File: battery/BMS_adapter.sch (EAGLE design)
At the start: 20 parts, among them J1 1376357-3

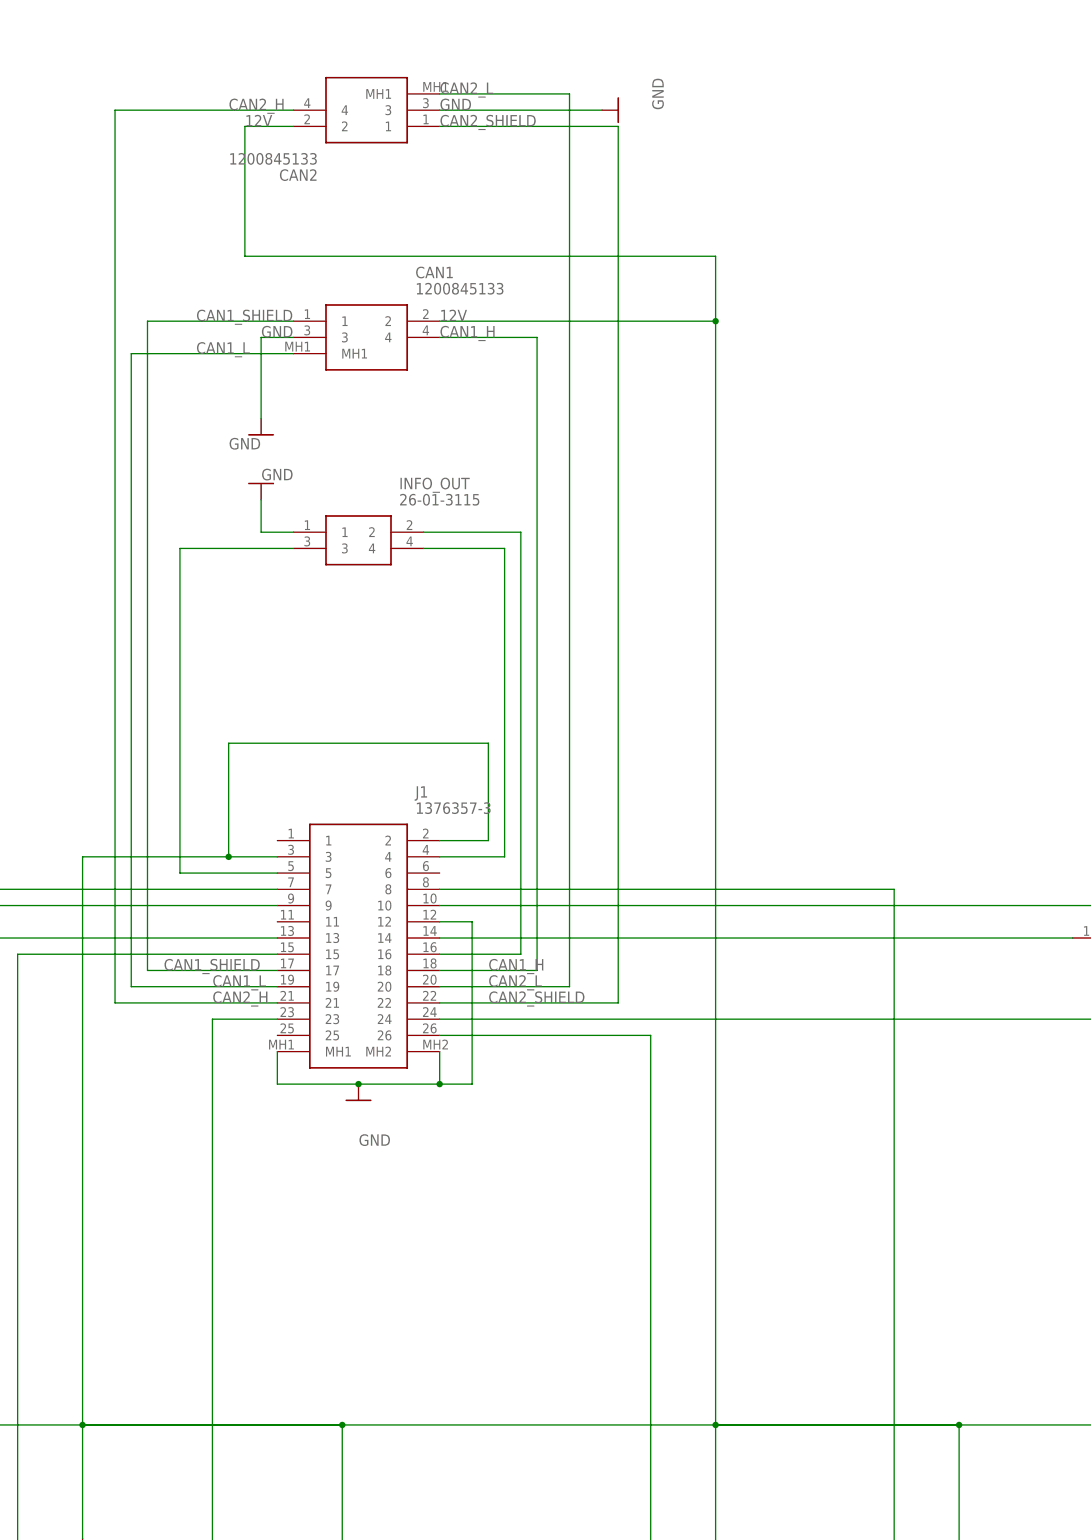
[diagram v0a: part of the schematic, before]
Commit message: changed linus' files to use the new BMS footprints.
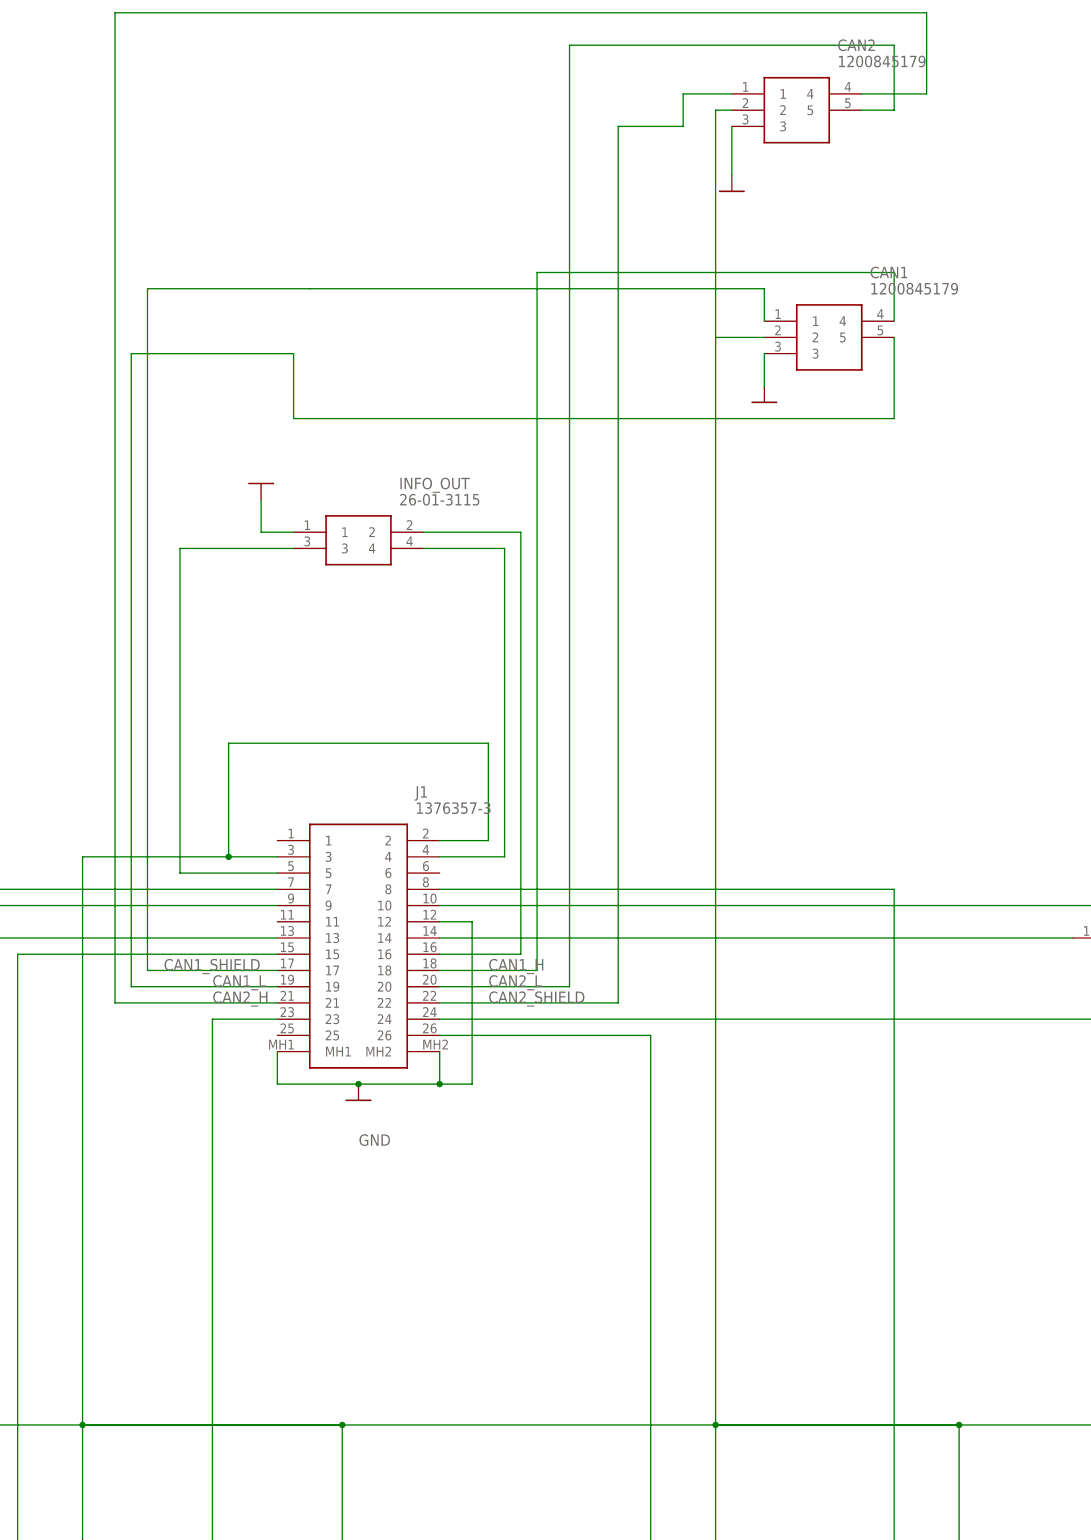
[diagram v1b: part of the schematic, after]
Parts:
- CAN1, CAN2: value 1200845133 -> 1200845179; device SamacSys_Parts:1200845133 -> SamacSys_Parts:1200845179
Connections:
- net CAN1_L: now also CAN1.5; no longer CAN1.MH1
- net CAN2_L: now also CAN2.5; no longer CAN2.MH1
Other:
- moved on the sheet: CAN1, CAN2
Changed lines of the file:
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@@
 <?xml version="1.0" encoding="utf-8"?>
 <!DOCTYPE eagle SYSTEM "eagle.dtd">
-<eagle version="9.1.1">
+<eagle version="9.1.3">
 <drawing>
 <settings>
@@
 <part name="MPO3" library="SamacSys_Parts" deviceset="26-01-3114" device=""/>
 <part name="MPO4" library="SamacSys_Parts" deviceset="26-01-3114" device=""/>
-<part name="CAN1" library="SamacSys_Parts" deviceset="1200845133" device=""/>
-<part name="GND2" library="SparkFun-PowerSymbols" library_urn="urn:adsk.eagle:library:530" deviceset="GND" device=""/>
-<part name="CAN2" library="SamacSys_Parts" deviceset="1200845133" device=""/>
-<part name="GND5" library="SparkFun-PowerSymbols" library_urn="urn:adsk.eagle:library:530" deviceset="GND" device=""/>
+<part name="CAN2" library="SamacSys_Parts" deviceset="1200845179" device=""/>
+<part name="CAN1" library="SamacSys_Parts" deviceset="1200845179" device=""/>
+<part name="GND6" library="SparkFun-PowerSymbols" library_urn="urn:adsk.eagle:library:530" deviceset="GND" device=""/>
+<part name="GND7" library="SparkFun-PowerSymbols" library_urn="urn:adsk.eagle:library:530" deviceset="GND" device=""/>
 </parts>
 <sheets>
@@
 <attribute name="VALUE" x="110.49" y="147.32" size="1.778" layer="96" align="center-left"/>
 </instance>
-<instance part="GND3" gate="1" x="88.9" y="149.86" smashed="yes" rot="R180">
-<attribute name="VALUE" x="86.36" y="155.194" size="1.778" layer="96" rot="R180" align="top-center"/>
-</instance>
+<instance part="GND3" gate="1" x="88.9" y="149.86" smashed="yes" rot="R180"/>
 <instance part="MPO3" gate="G$1" x="236.22" y="83.82" smashed="yes">
 <attribute name="NAME" x="252.73" y="91.44" size="1.778" layer="95" align="center-left"/>
@@
 <attribute name="VALUE" x="252.73" y="71.12" size="1.778" layer="96" align="center-left"/>
 </instance>
-<instance part="CAN1" gate="G$1" x="93.98" y="175.26" smashed="yes">
-<attribute name="NAME" x="113.03" y="182.88" size="1.778" layer="95" align="center-left"/>
-<attribute name="VALUE" x="113.03" y="180.34" size="1.778" layer="96" align="center-left"/>
-</instance>
-<instance part="GND2" gate="1" x="88.9" y="157.48" smashed="yes">
-<attribute name="VALUE" x="91.44" y="152.146" size="1.778" layer="96" align="top-center"/>
-</instance>
-<instance part="CAN2" gate="G$1" x="116.84" y="205.74" smashed="yes" rot="R180">
-<attribute name="NAME" x="97.79" y="198.12" size="1.778" layer="95" rot="R180" align="center-left"/>
-<attribute name="VALUE" x="97.79" y="200.66" size="1.778" layer="96" rot="R180" align="center-left"/>
-</instance>
-<instance part="GND5" gate="1" x="144.78" y="208.28" smashed="yes" rot="R90">
-<attribute name="VALUE" x="150.114" y="210.82" size="1.778" layer="96" rot="R90" align="top-center"/>
-</instance>
+<instance part="CAN2" gate="G$1" x="162.56" y="210.82"/>
+<instance part="CAN1" gate="G$1" x="167.64" y="175.26"/>
+<instance part="GND6" gate="1" x="162.56" y="195.58" smashed="yes"/>
+<instance part="GND7" gate="1" x="167.64" y="162.56" smashed="yes"/>
 </instances>
 <busses>
@@
 </segment>
 <segment>
-<pinref part="GND2" gate="1" pin="GND"/>
+<pinref part="CAN2" gate="G$1" pin="3"/>
+<wire x1="162.56" y1="205.74" x2="162.56" y2="198.12" width="0.1524" layer="91"/>
+<pinref part="GND6" gate="1" pin="GND"/>
+</segment>
+<segment>
 <pinref part="CAN1" gate="G$1" pin="3"/>
-<wire x1="93.98" y1="172.72" x2="88.9" y2="172.72" width="0.1524" layer="91"/>
-<wire x1="88.9" y1="172.72" x2="88.9" y2="160.02" width="0.1524" layer="91"/>
-<label x="88.9" y="172.72" size="1.778" layer="95"/>
-</segment>
-<segment>
-<pinref part="GND5" gate="1" pin="GND"/>
-<pinref part="CAN2" gate="G$1" pin="3"/>
-<wire x1="116.84" y1="208.28" x2="142.24" y2="208.28" width="0.1524" layer="91"/>
-<label x="116.84" y="208.28" size="1.778" layer="95"/>
+<wire x1="167.64" y1="170.18" x2="167.64" y2="165.1" width="0.1524" layer="91"/>
+<pinref part="GND7" gate="1" pin="GND"/>
 </segment>
 </net>
@@
 <wire x1="17.78" y1="-17.78" x2="17.78" y2="2.54" width="0.1524" layer="91"/>
 <wire x1="60.96" y1="91.44" x2="60.96" y2="2.54" width="0.1524" layer="91"/>
+<wire x1="160.02" y1="2.54" x2="160.02" y2="172.72" width="0.1524" layer="91"/>
+<wire x1="160.02" y1="172.72" x2="160.02" y2="208.28" width="0.1524" layer="91"/>
+<pinref part="CAN2" gate="G$1" pin="2"/>
+<wire x1="160.02" y1="208.28" x2="162.56" y2="208.28" width="0.1524" layer="91"/>
 <pinref part="CAN1" gate="G$1" pin="2"/>
-<wire x1="160.02" y1="2.54" x2="160.02" y2="175.26" width="0.1524" layer="91"/>
-<wire x1="160.02" y1="175.26" x2="116.84" y2="175.26" width="0.1524" layer="91"/>
-<pinref part="CAN2" gate="G$1" pin="2"/>
-<wire x1="93.98" y1="205.74" x2="86.36" y2="205.74" width="0.1524" layer="91"/>
-<wire x1="86.36" y1="205.74" x2="86.36" y2="185.42" width="0.1524" layer="91"/>
-<wire x1="86.36" y1="185.42" x2="160.02" y2="185.42" width="0.1524" layer="91"/>
-<wire x1="160.02" y1="185.42" x2="160.02" y2="175.26" width="0.1524" layer="91"/>
-<junction x="160.02" y="175.26"/>
-<label x="116.84" y="175.26" size="1.778" layer="95"/>
-<label x="86.36" y="205.74" size="1.778" layer="95"/>
+<wire x1="160.02" y1="172.72" x2="167.64" y2="172.72" width="0.1524" layer="91"/>
 </segment>
 </net>
@@
 <pinref part="J1" gate="G$1" pin="17"/>
 <wire x1="91.44" y1="73.66" x2="71.12" y2="73.66" width="0.1524" layer="91"/>
-<wire x1="71.12" y1="73.66" x2="71.12" y2="175.26" width="0.1524" layer="91"/>
+<wire x1="71.12" y1="73.66" x2="71.12" y2="180.34" width="0.1524" layer="91"/>
+<wire x1="71.12" y1="180.34" x2="96.52" y2="180.34" width="0.1524" layer="91"/>
+<label x="73.66" y="73.66" size="1.778" layer="95"/>
+<wire x1="96.52" y1="180.34" x2="167.64" y2="180.34" width="0.1524" layer="91"/>
 <pinref part="CAN1" gate="G$1" pin="1"/>
-<wire x1="71.12" y1="175.26" x2="93.98" y2="175.26" width="0.1524" layer="91"/>
-<label x="73.66" y="73.66" size="1.778" layer="95"/>
-<label x="78.74" y="175.26" size="1.778" layer="95"/>
+<wire x1="167.64" y1="180.34" x2="167.64" y2="175.26" width="0.1524" layer="91"/>
 </segment>
 </net>
@@
 <pinref part="J1" gate="G$1" pin="18"/>
 <wire x1="116.84" y1="73.66" x2="132.08" y2="73.66" width="0.1524" layer="91"/>
+<wire x1="132.08" y1="73.66" x2="132.08" y2="182.88" width="0.1524" layer="91"/>
+<label x="124.46" y="73.66" size="1.778" layer="95"/>
+<wire x1="132.08" y1="182.88" x2="187.96" y2="182.88" width="0.1524" layer="91"/>
 <pinref part="CAN1" gate="G$1" pin="4"/>
-<wire x1="132.08" y1="73.66" x2="132.08" y2="172.72" width="0.1524" layer="91"/>
-<wire x1="132.08" y1="172.72" x2="116.84" y2="172.72" width="0.1524" layer="91"/>
-<label x="124.46" y="73.66" size="1.778" layer="95"/>
-<label x="116.84" y="172.72" size="1.778" layer="95"/>
+<wire x1="187.96" y1="182.88" x2="187.96" y2="175.26" width="0.1524" layer="91"/>
 </segment>
 </net>
@@
 <wire x1="91.44" y1="71.12" x2="68.58" y2="71.12" width="0.1524" layer="91"/>
 <wire x1="68.58" y1="71.12" x2="68.58" y2="170.18" width="0.1524" layer="91"/>
-<pinref part="CAN1" gate="G$1" pin="MH1"/>
 <wire x1="68.58" y1="170.18" x2="93.98" y2="170.18" width="0.1524" layer="91"/>
 <label x="81.28" y="71.12" size="1.778" layer="95"/>
-<label x="78.74" y="170.18" size="1.778" layer="95"/>
+<wire x1="93.98" y1="170.18" x2="93.98" y2="160.02" width="0.1524" layer="91"/>
+<pinref part="CAN1" gate="G$1" pin="5"/>
+<wire x1="93.98" y1="160.02" x2="187.96" y2="160.02" width="0.1524" layer="91"/>
+<wire x1="187.96" y1="160.02" x2="187.96" y2="172.72" width="0.1524" layer="91"/>
 </segment>
 </net>
@@
 <wire x1="116.84" y1="68.58" x2="144.78" y2="68.58" width="0.1524" layer="91"/>
 <wire x1="144.78" y1="68.58" x2="144.78" y2="205.74" width="0.1524" layer="91"/>
+<label x="124.46" y="68.58" size="1.778" layer="95"/>
+<wire x1="144.78" y1="205.74" x2="154.94" y2="205.74" width="0.1524" layer="91"/>
+<wire x1="154.94" y1="205.74" x2="154.94" y2="210.82" width="0.1524" layer="91"/>
 <pinref part="CAN2" gate="G$1" pin="1"/>
-<wire x1="144.78" y1="205.74" x2="116.84" y2="205.74" width="0.1524" layer="91"/>
-<label x="124.46" y="68.58" size="1.778" layer="95"/>
-<label x="116.84" y="205.74" size="1.778" layer="95"/>
+<wire x1="154.94" y1="210.82" x2="162.56" y2="210.82" width="0.1524" layer="91"/>
 </segment>
 </net>
@@
 <pinref part="J1" gate="G$1" pin="21"/>
 <wire x1="91.44" y1="68.58" x2="66.04" y2="68.58" width="0.1524" layer="91"/>
-<wire x1="66.04" y1="68.58" x2="66.04" y2="208.28" width="0.1524" layer="91"/>
+<wire x1="66.04" y1="68.58" x2="66.04" y2="223.52" width="0.1524" layer="91"/>
+<label x="81.28" y="68.58" size="1.778" layer="95"/>
+<wire x1="66.04" y1="223.52" x2="193.04" y2="223.52" width="0.1524" layer="91"/>
+<wire x1="193.04" y1="223.52" x2="193.04" y2="210.82" width="0.1524" layer="91"/>
 <pinref part="CAN2" gate="G$1" pin="4"/>
-<wire x1="66.04" y1="208.28" x2="93.98" y2="208.28" width="0.1524" layer="91"/>
-<label x="81.28" y="68.58" size="1.778" layer="95"/>
-<label x="83.82" y="208.28" size="1.778" layer="95"/>
+<wire x1="193.04" y1="210.82" x2="182.88" y2="210.82" width="0.1524" layer="91"/>
 </segment>
 </net>
@@
 <pinref part="J1" gate="G$1" pin="20"/>
 <wire x1="116.84" y1="71.12" x2="137.16" y2="71.12" width="0.1524" layer="91"/>
-<wire x1="137.16" y1="71.12" x2="137.16" y2="210.82" width="0.1524" layer="91"/>
-<pinref part="CAN2" gate="G$1" pin="MH1"/>
-<wire x1="137.16" y1="210.82" x2="116.84" y2="210.82" width="0.1524" layer="91"/>
+<wire x1="137.16" y1="71.12" x2="137.16" y2="218.44" width="0.1524" layer="91"/>
 <label x="124.46" y="71.12" size="1.778" layer="95"/>
-<label x="116.84" y="210.82" size="1.778" layer="95"/>
-</segment>
-</net>
+<wire x1="137.16" y1="218.44" x2="187.96" y2="218.44" width="0.1524" layer="91"/>
+<wire x1="187.96" y1="218.44" x2="187.96" y2="208.28" width="0.1524" layer="91"/>
+<pinref part="CAN2" gate="G$1" pin="5"/>
+<wire x1="187.96" y1="208.28" x2="182.88" y2="208.28" width="0.1524" layer="91"/>
+</segment>
+</net>
